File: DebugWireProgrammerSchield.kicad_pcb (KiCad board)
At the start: 2 copper layers, 57.7 x 20.1 mm, 17 parts, among them J1 Conn_01x15, J2 Conn_01x15, J3 ISCP, Q1 TP2104, Q2 Q_NPN_BCE, SW1 SW_SPDT, U1 ATtiny85

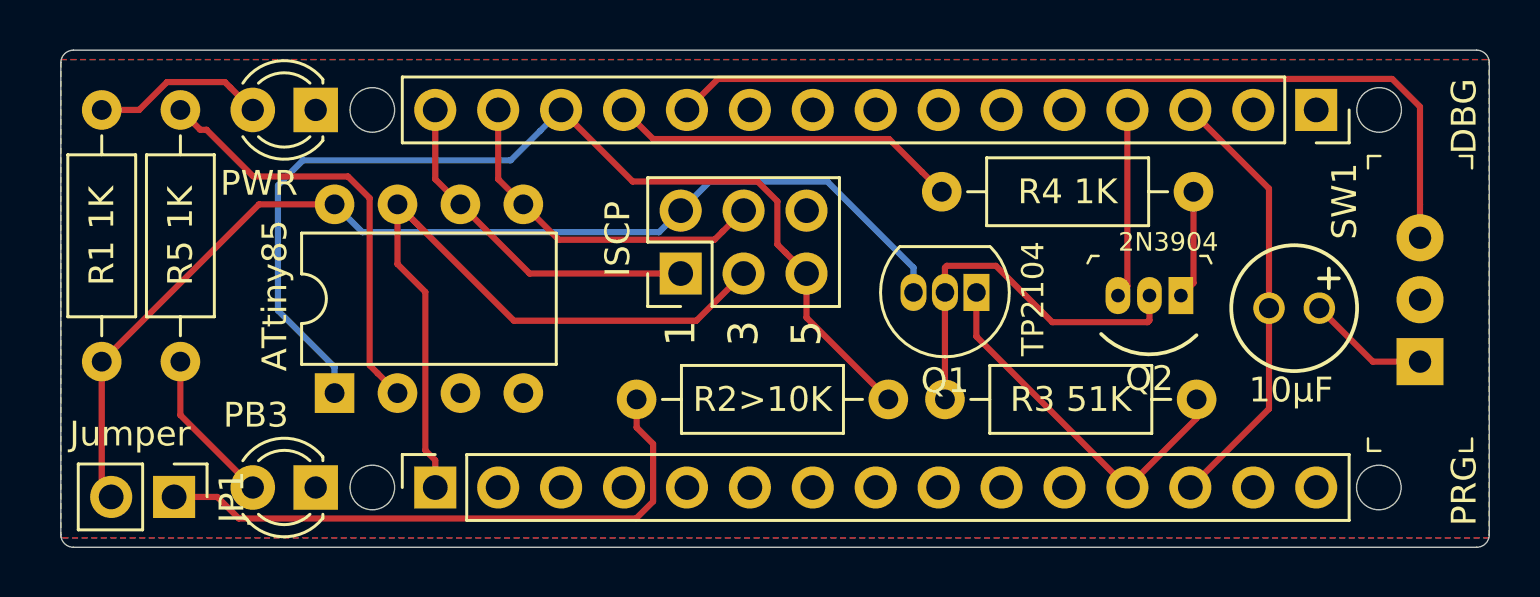
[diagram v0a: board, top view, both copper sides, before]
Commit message: cleanup silkscreen typos
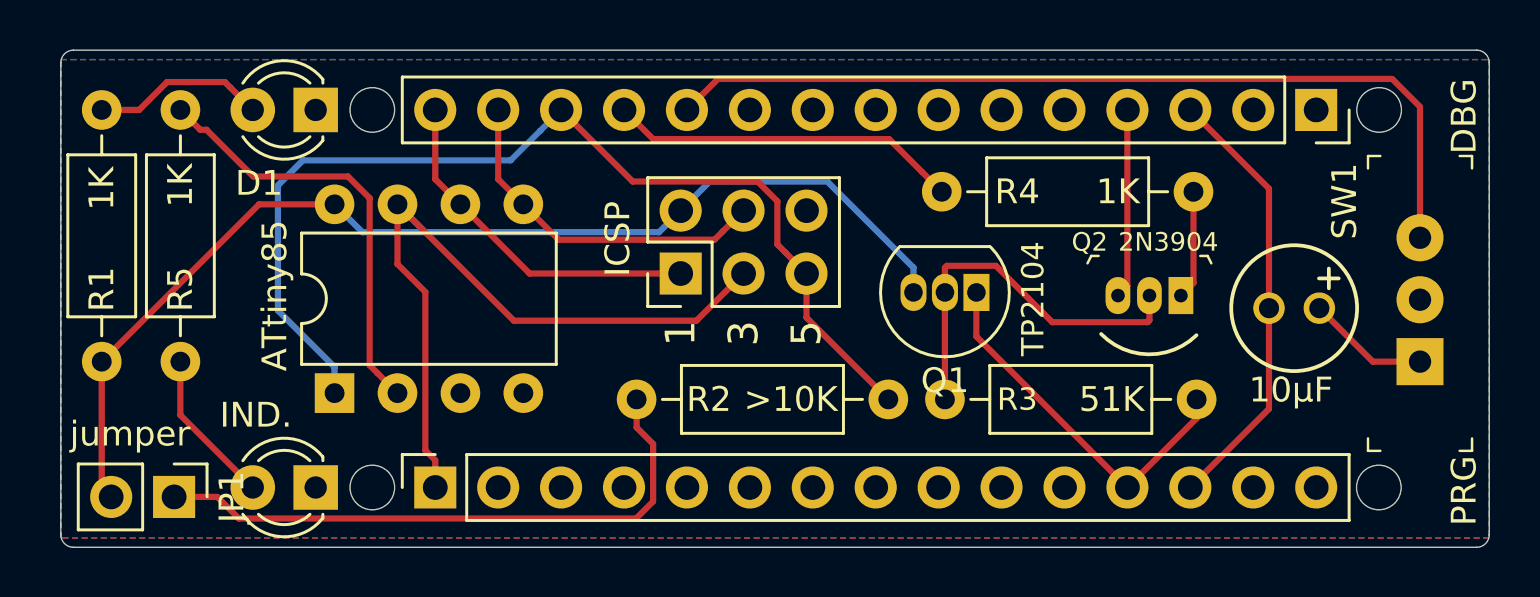
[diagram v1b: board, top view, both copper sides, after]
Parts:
- D1: renamed from PWR; value LED -> PWR
- D2: value PB3 -> IND.
- J3: value ISCP -> ICSP
- JP1: value Jumper -> jumper
- Q2: value Q_NPN_BCE -> 2N3904
- R4: renamed from R4 1K
- R5: renamed from R5 1K
- SW1: value SW_SPDT -> PRG/DBG
- renumbered R2>10K to R2
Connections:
- net Net-(C1-Pad1) renamed /PROG

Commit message: update info for Rev 2.0
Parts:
- moved D1 0.13 mm to (140.2, 77.6)
- moved D2 0.13 mm to (140.2, 92.8)
- moved R1 0.13 mm to (131.6, 87.8)
- moved R5 0.13 mm to (134.7, 77.6)
- moved JP1 0.13 mm to (134.5, 93.2)
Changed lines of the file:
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@@
   (title_block
     (title "DebugWireDebuggerProgrammer Arduino Nano Shield")
-    (date 2021-02-12)
-    (rev 1.0)
+    (date 2021-02-13)
+    (rev 2.0)
     (comment 1 "Author: Joost Oostdijk")
   )
@@
   )
   (module Resistor_THT:R_Axial_DIN0207_L6.3mm_D2.5mm_P10.16mm_Horizontal (layer F.Cu)
-    (at 134.62 77.597 270)
+    (at 134.747 77.597 270)
     (descr "Resistor, Axial_DIN0207 series, Axial, Horizontal, pin pitch=10.16mm, 0.25W = 1/4W, length*diameter=6.3*2.5mm^2, http://cdn-reichelt.de/documents/datenblatt/B400/1_4W%23YAG.pdf")
     (tags "Resistor Axial_DIN0207 series Axial Horizontal pin pitch 10.16mm 0.25W = 1/4W length 6.3mm diameter 2.5mm")
@@
   )
   (module Resistor_THT:R_Axial_DIN0207_L6.3mm_D2.5mm_P10.16mm_Horizontal (layer F.Cu)
-    (at 131.445 87.757 90)
+    (at 131.572 87.757 90)
     (descr "Resistor, Axial_DIN0207 series, Axial, Horizontal, pin pitch=10.16mm, 0.25W = 1/4W, length*diameter=6.3*2.5mm^2, http://cdn-reichelt.de/documents/datenblatt/B400/1_4W%23YAG.pdf")
     (tags "Resistor Axial_DIN0207 series Axial Horizontal pin pitch 10.16mm 0.25W = 1/4W length 6.3mm diameter 2.5mm")
@@
     (descr "TO-92 leads in-line, narrow, oval pads, drill 0.75mm (see NXP sot054_po.pdf)")
     (tags "to-92 sc-43 sc-43a sot54 PA33 transistor")
-    (fp_text reference Q1 (at 1.27 -3.56) (layer F.SilkS)
+    (fp_text reference Q1 (at 3.683 2.667) (layer F.SilkS)
       (effects (font (size 1 1) (thickness 0.15)))
     )
@@
   )
   (module Connector_PinHeader_2.54mm:PinHeader_1x02_P2.54mm_Vertical (layer F.Cu)
-    (at 134.366 93.218 270)
+    (at 134.493 93.218 270)
     (descr "Through hole straight pin header, 1x02, 2.54mm pitch, single row")
     (tags "Through hole pin header THT 1x02 2.54mm single row")
@@
   )
   (module LED_THT:LED_D3.0mm (layer F.Cu)
-    (at 140.081 92.837 180)
+    (at 140.208 92.837 180)
     (descr "LED, diameter 3.0mm, 2 pins")
     (tags "LED diameter 3.0mm 2 pins")
@@
   )
   (module LED_THT:LED_D3.0mm (layer F.Cu)
-    (at 140.081 77.597 180)
+    (at 140.208 77.597 180)
     (descr "LED, diameter 3.0mm, 2 pins")
     (tags "LED diameter 3.0mm 2 pins")
